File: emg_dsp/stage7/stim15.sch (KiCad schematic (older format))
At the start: 32 parts, among them U1 10X100, U10 IL715-3, U11 IL715-3, U2 MCP4017, U3 6533-CONN, U4 IL715-3, U5 IL715-3, U6 IL715-3, U7 IL715-3, U8 IL715-3, U9 IL715-3

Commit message: adding changes to new board -- still feel that the schematic needs to be checked over, though.
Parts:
- renumbered C1 to C70, C2 to C71, C3 to C72, C4 to C73, C5 to C74, C6 to C75, C7 to C76, C8 to C77, C9 to C78, C10 to C79, C11 to C80, C12 to C81, C13 to C82, C14 to C83, C15 to C84, C16 to C85, C17 to C86, R1 to R66, R2 to R67, R4 to R68, R3 to R69, U1 to U31, U2 to U32, U3 to U33, U4 to U34, U5 to U35, U6 to U36, U7 to U37, U8 to U38, U9 to U39, U10 to U40, U11 to U41

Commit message: working on the stimulator - using battery isolation for now. the Burr-brown DC-DC converters tend to generate a bit of noise.
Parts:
- added C? (x2): 33pf, 0402, symbol C
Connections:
- net labels added: IGND, VBAT
- net labels removed: CGND
- wire segments 212 -> 252

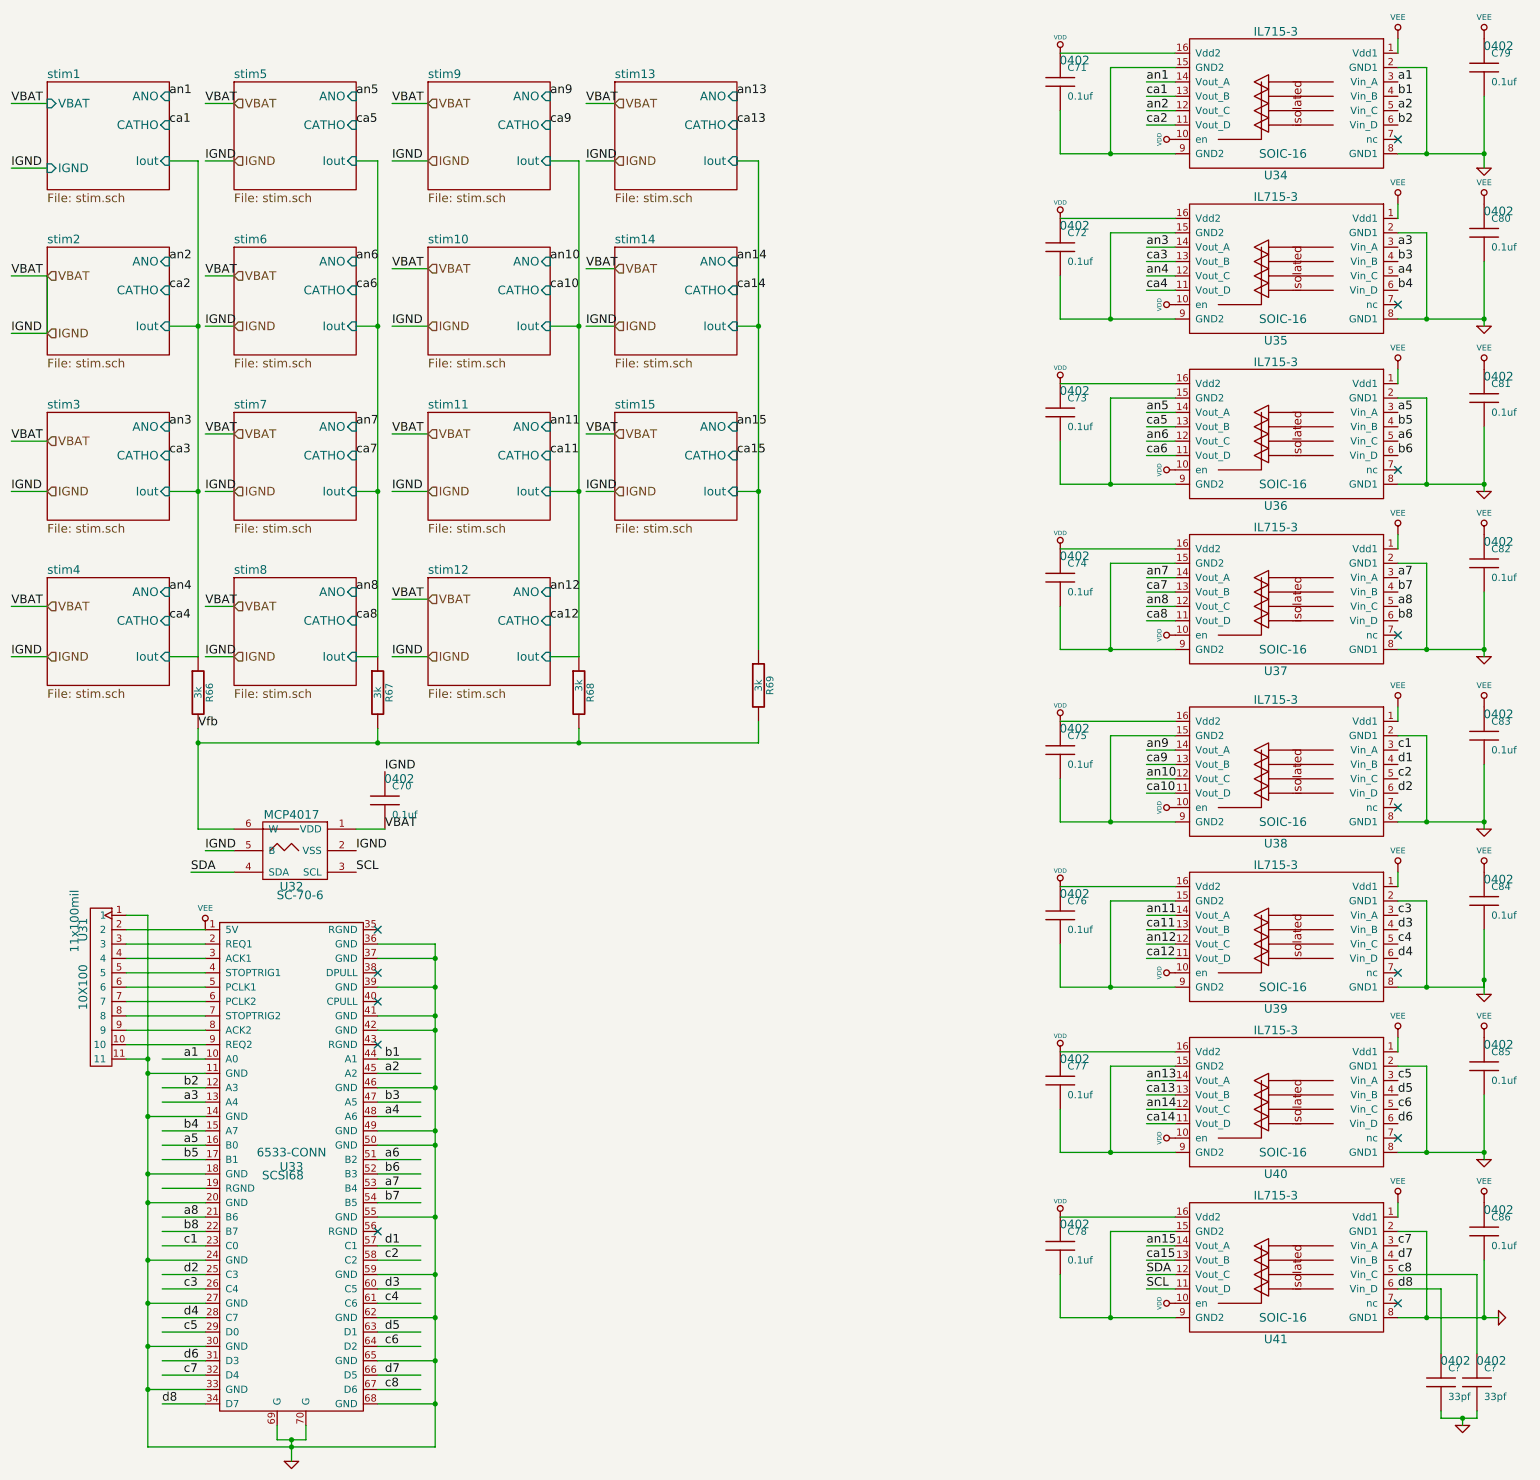
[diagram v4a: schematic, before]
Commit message: starting placement of modules in board...
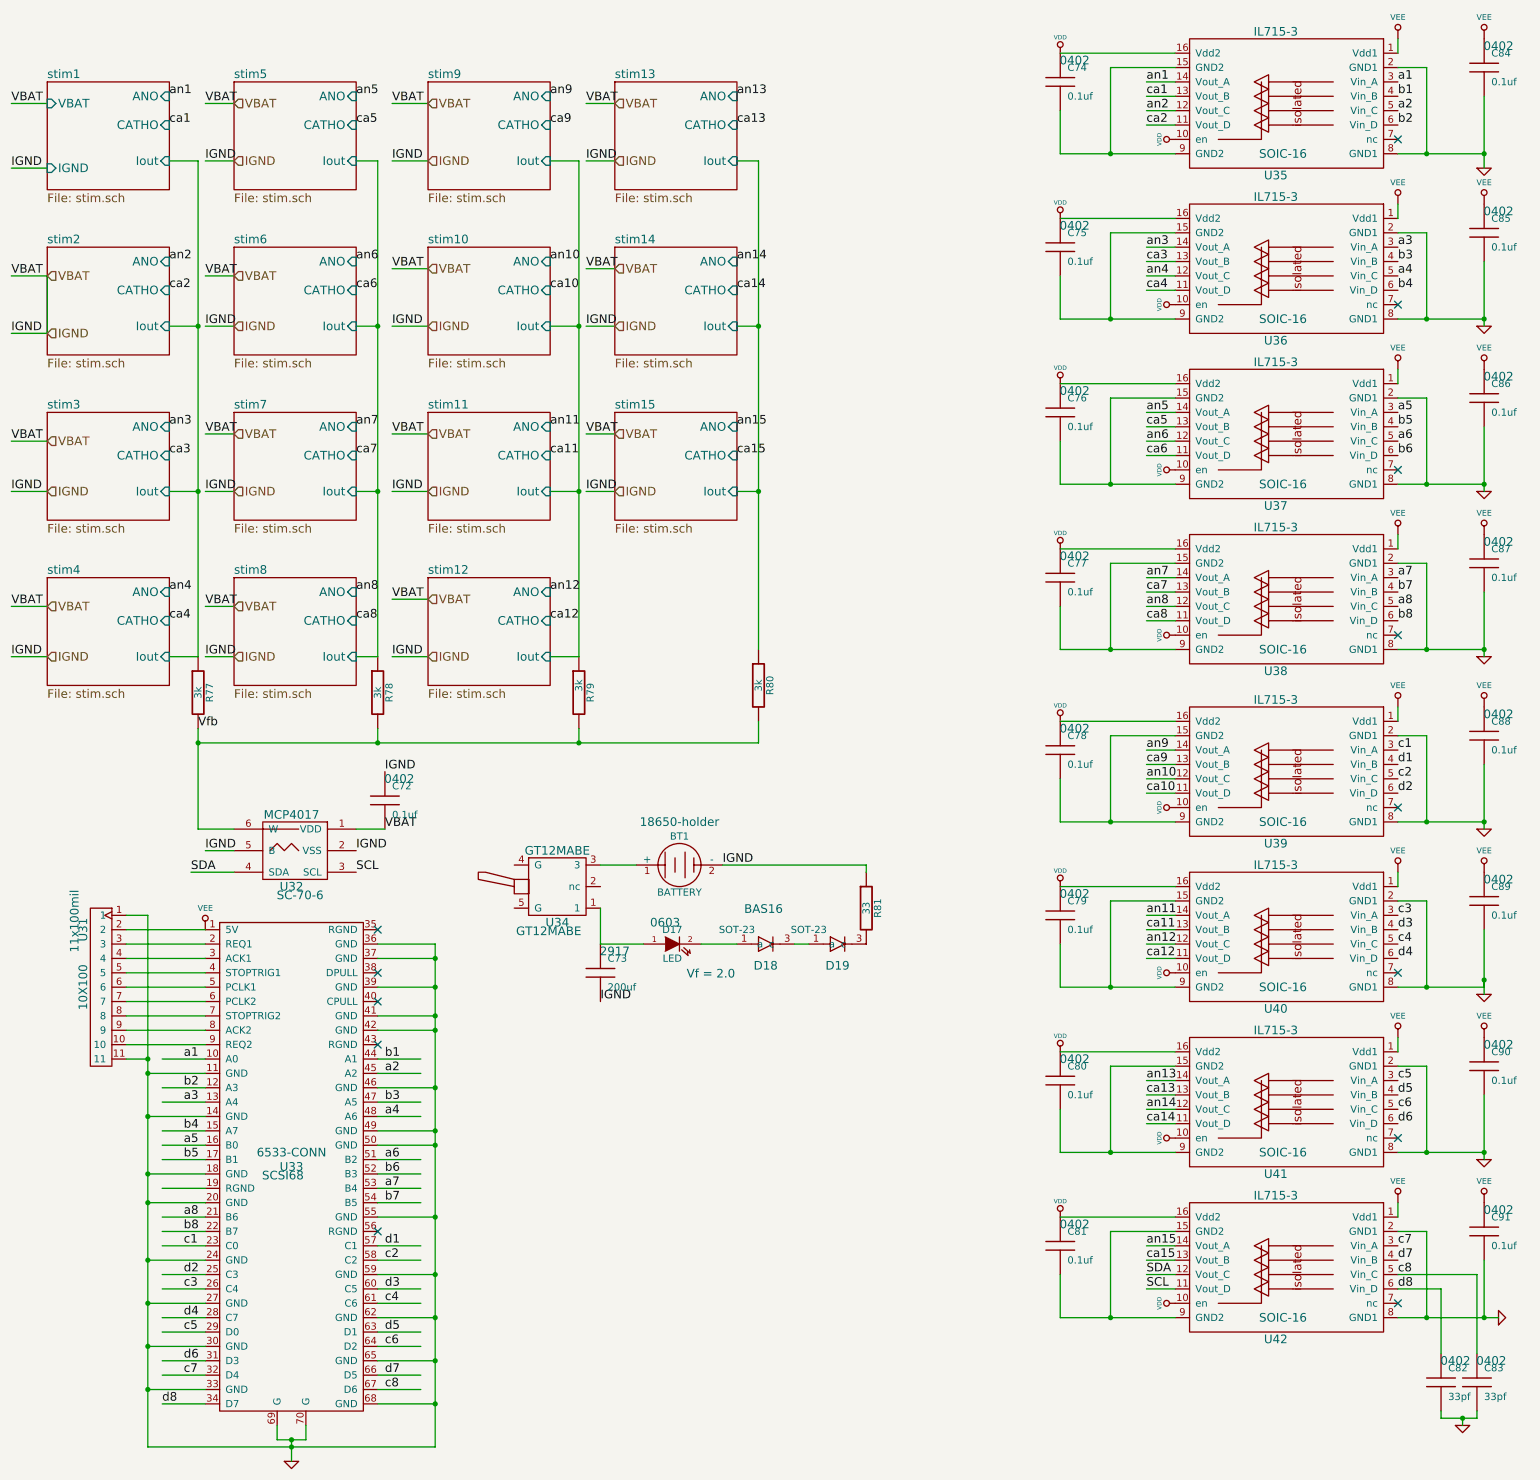
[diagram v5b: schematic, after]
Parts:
- added BT1: BATTERY, 18650-holder, symbol BATTERY
- added C73: 200uf, 2917, symbol C
- added D17: LED, 0603, symbol LED
- added D18, D19: D, SOT-23, symbol D
- added R81: 33, 0402, symbol R
- added U34: GT12MABE, GT12MABE, symbol GT12MABE
- gave numbers to parts that had none: 2
- renumbered C70 to C72, C71 to C74, C72 to C75, C73 to C76, C74 to C77, C75 to C78, C76 to C79, C77 to C80, C78 to C81, C79 to C84, C80 to C85, C81 to C86, C82 to C87, C83 to C88, C84 to C89, C85 to C90, C86 to C91, R66 to R77, R67 to R78, R68 to R79, R69 to R80, U34 to U35, U35 to U36, U36 to U37, U37 to U38, U38 to U39, U39 to U40, U40 to U41, U41 to U42
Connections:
- wire segments 252 -> 259
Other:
- note added: "BAS16"
- note added: "Vf = 2.0"

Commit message: placed modules in stim and wired, issues with shorting in stims
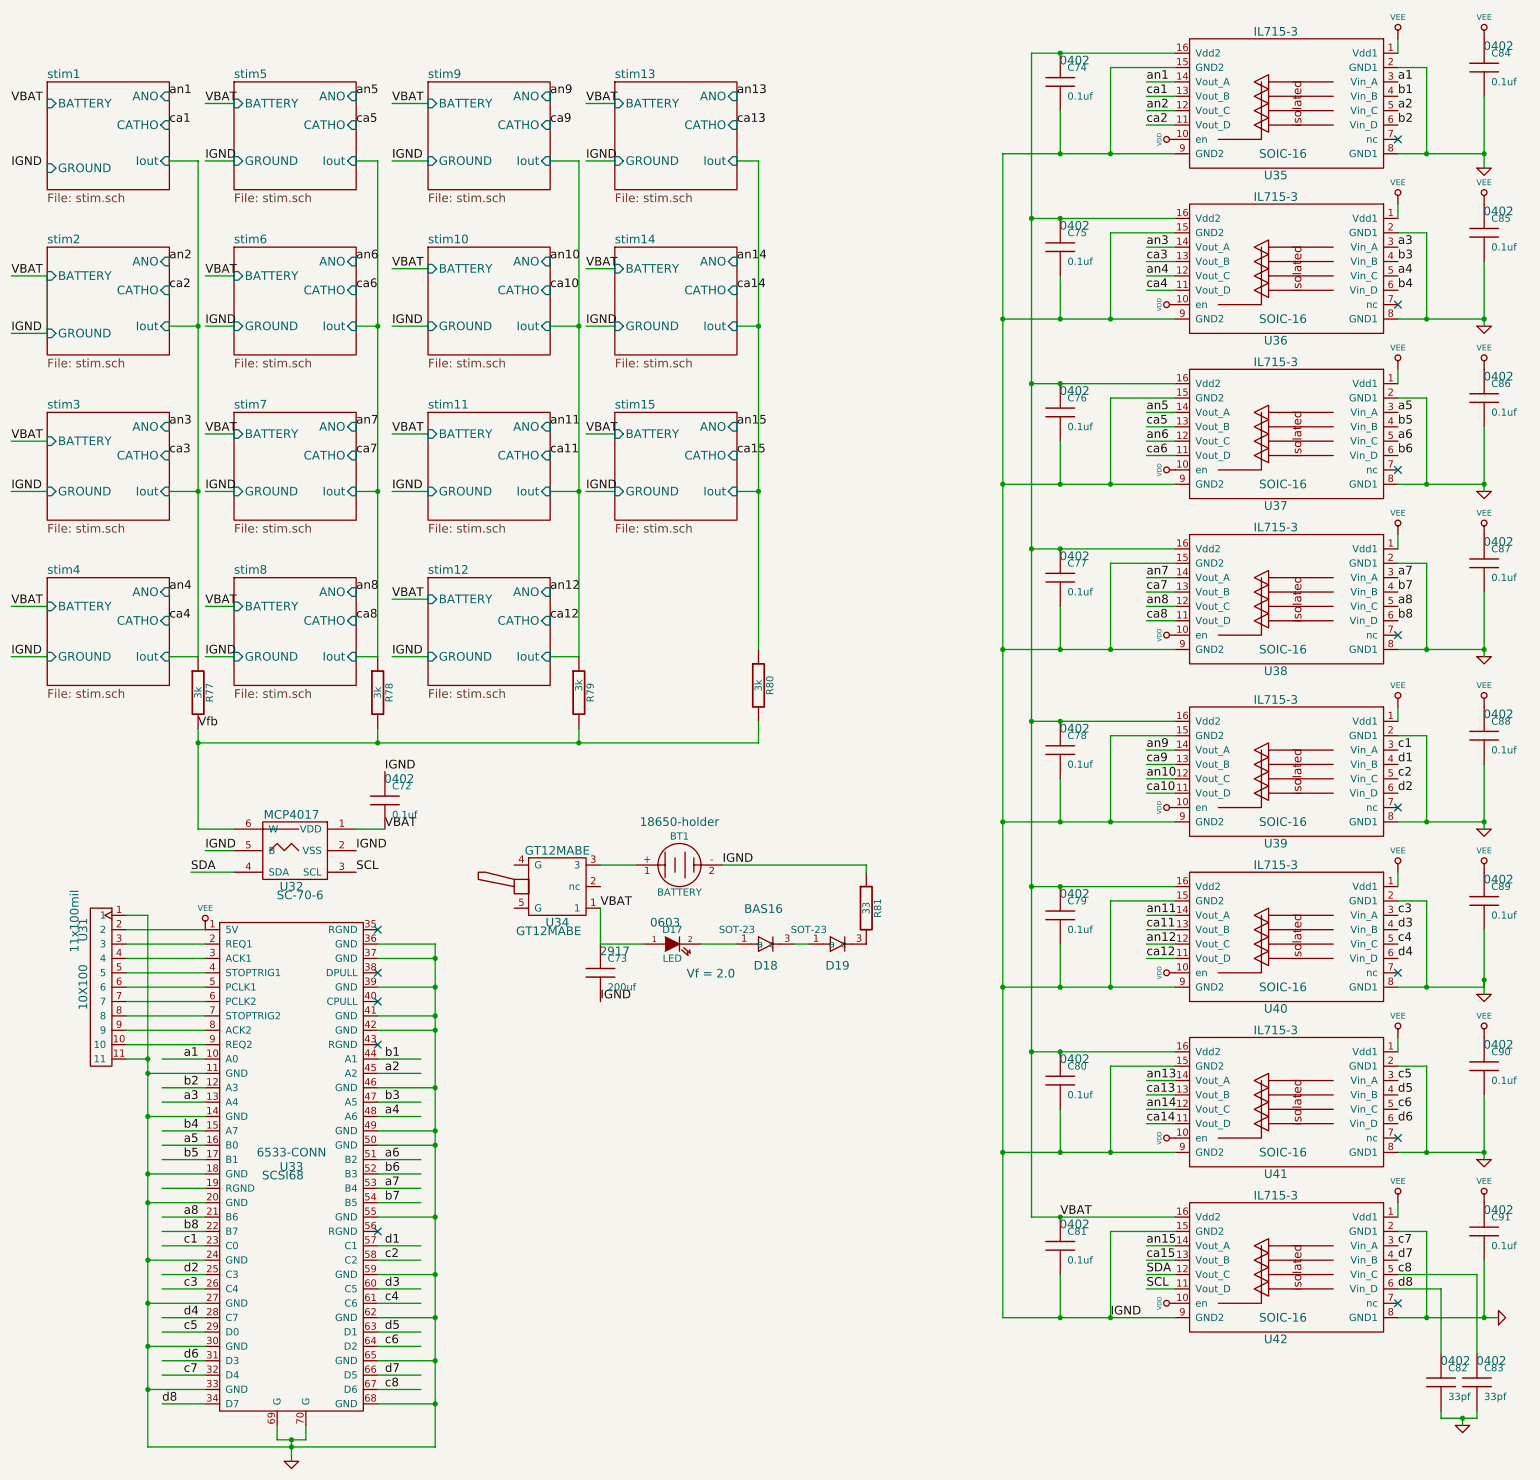
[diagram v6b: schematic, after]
